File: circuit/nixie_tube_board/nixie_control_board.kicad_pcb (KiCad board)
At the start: 4 copper layers, 200 x 63 mm, 11 parts, among them P5 CONN_01X08, P6 CONN_01X12, U10 IN-14, U11 IN-14, U12 IN-14, U13 IN-14, U14 IN-14, U15 IN-14, U16 IN-14, U17 IN-14

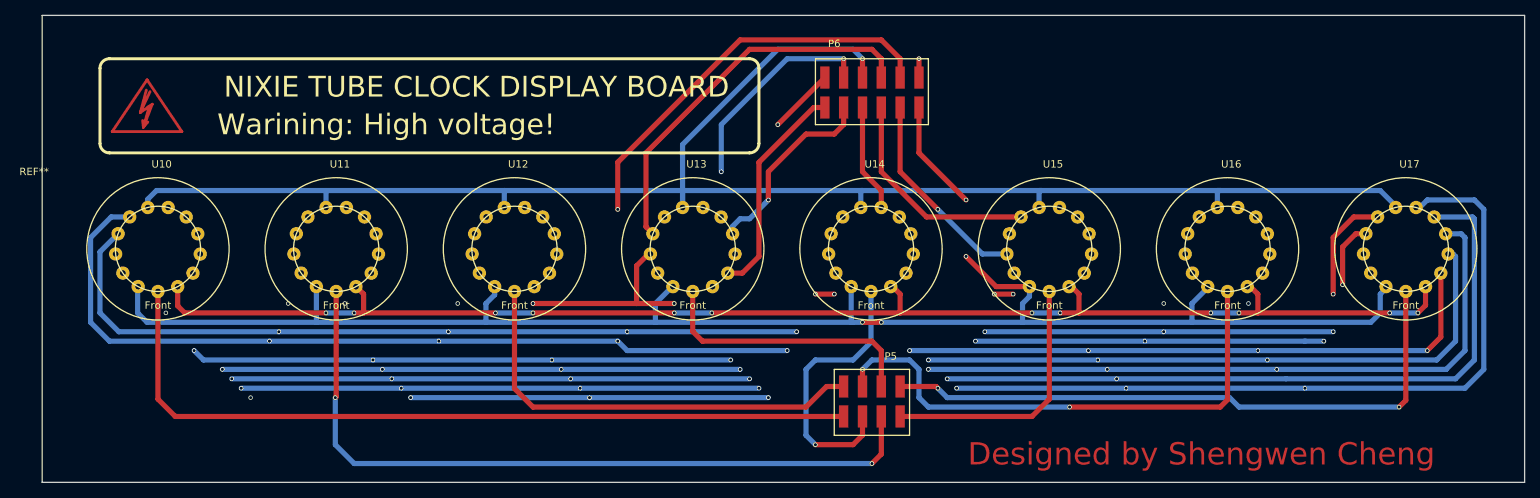
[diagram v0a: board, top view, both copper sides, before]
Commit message: New hardware is almost finished
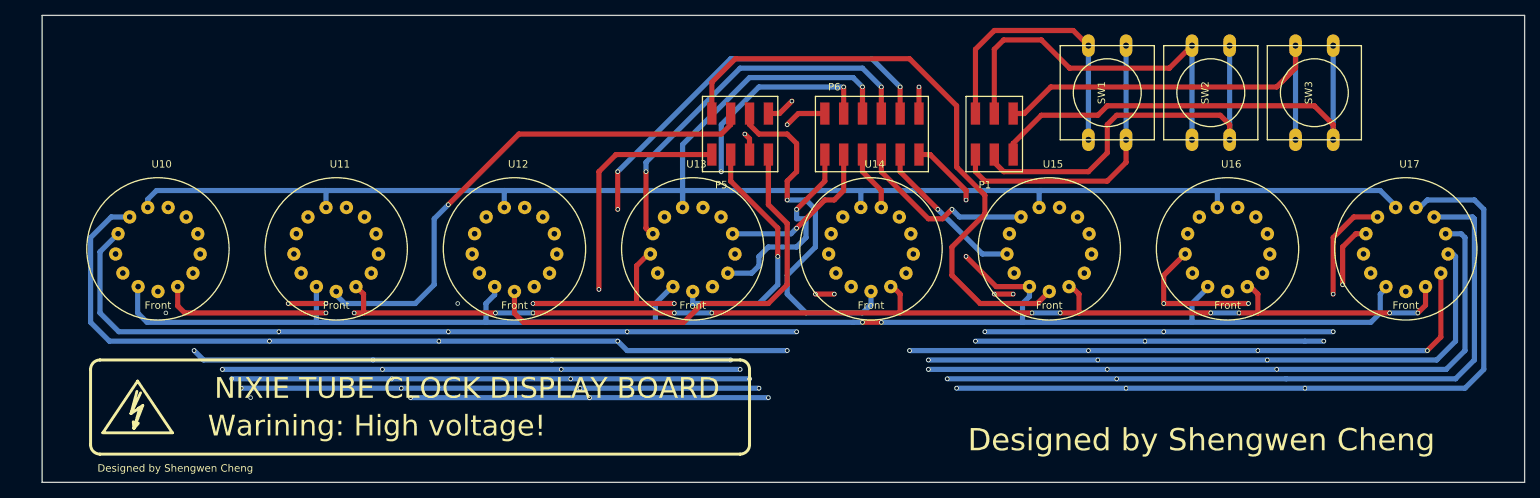
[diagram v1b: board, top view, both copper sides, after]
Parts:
- removed REF**: Symbol_HighVoltage_Type2_CopperTop_VerySmall, Symbols:Symbol_HighVoltage_Type2_CopperTop_VerySmall
- added Designed by Shengwen Cheng: Symbol_HighVoltage_Type2_CopperTop_VerySmall, warning:warning, F.Cu at (65.0, 124.1)
- added P1: CONN_02X03, SMD_PIN_2_BY_3:SMD_PIN_2_BY_3, F.Cu at (178.0, 85.3)
- added SW1: SW_PUSH, Buttons_Switches_ThroughHole:SW_PUSH-12mm, F.Cu at (195.8, 81.0)
- added SW2: SW_PUSH, Buttons_Switches_ThroughHole:SW_PUSH-12mm, F.Cu at (209.7, 81.0)
- added SW3: SW_PUSH, Buttons_Switches_ThroughHole:SW_PUSH-12mm, F.Cu at (223.7, 81.0)
- moved P5 46.9 mm to (142.4, 85.3), turned to 0 degrees
- moved P6 6.35 mm to (157.7, 85.3)
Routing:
- net anode8: track 84.4 -> 168.3 mm, vias 2 -> 1
- net Net-(P1-Pad5): track 0.00 -> 62.6 mm
- net Net-(P1-Pad6): track 0.00 -> 56.4 mm
- net Net-(P1-Pad3): track 0.00 -> 54.0 mm
- net Net-(P1-Pad4): track 0.00 -> 51.4 mm
- net anode7: track 35.6 -> 82.8 mm
- net Net-(P1-Pad1): track 0.00 -> 39.9 mm
- net Net-(P1-Pad2): track 0.00 -> 38.5 mm
- net anode5: track 101.0 -> 70.9 mm, vias 2 -> 1
- net anode4: track 72.0 -> 96.7 mm, vias 2 -> 1
- net anode3: track 37.2 -> 49.0 mm
- net cathode6: track 452.8 -> 446.5 mm
- net cathode2: track 257.0 -> 251.1 mm
- net cathode4: track 365.2 -> 359.9 mm, vias 8 -> 9
- net cathode_comma_left: track 241.1 -> 236.0 mm
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
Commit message: Create footprint common library
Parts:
- removed Designed by Shengwen Cheng: Symbol_HighVoltage_Type2_CopperTop_VerySmall, warning:warning
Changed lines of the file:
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@@
     (links 116)
     (no_connects 3)
-    (area 48.908353 70.493439 252.145001 133.643441)
+    (area 51.994999 70.493439 252.145001 133.643441)
     (thickness 1.6)
     (drawings 15)
     (tracks 738)
     (zones 0)
-    (modules 15)
+    (modules 14)
     (nets 27)
   )
@@
       (net 13 cathode9))
   )
-  (module warning:warning (layer F.Cu)
-    (at 64.95288 124.09)
-    (descr "Symbol, High Voltage, Type 2, Copper Top, Very Small,")
-    (tags "Symbol, High Voltage, Type 2, Copper Top, Very Small,")
-    (fp_text reference "Designed by Shengwen Cheng" (at 5.08 7.57344) (layer F.SilkS)
-      (effects (font (size 1 1) (thickness 0.15)))
-    )
-    (fp_text value Symbol_HighVoltage_Type2_CopperTop_VerySmall (at 2.54 -10.16) (layer F.Fab)
-      (effects (font (size 1 1) (thickness 0.15)))
-    )
-    (fp_line (start -0.49784 2.19964) (end 0.70104 -0.89916) (layer F.SilkS) (width 0.381))
-    (fp_line (start 0.70104 -0.89916) (end 0.1016 -0.50038) (layer F.SilkS) (width 0.381))
-    (fp_line (start -0.89916 0.20066) (end 0.40132 -2.60096) (layer F.SilkS) (width 0.381))
-    (fp_line (start -0.49784 2.19964) (end 0.1016 1.50114) (layer F.SilkS) (width 0.381))
-    (fp_line (start -0.09906 -2.79908) (end -0.89916 0.20066) (layer F.SilkS) (width 0.381))
-    (fp_line (start -0.89916 0.20066) (end 0.29972 -0.59944) (layer F.SilkS) (width 0.381))
-    (fp_line (start 0.29972 -0.59944) (end -0.49784 2.19964) (layer F.SilkS) (width 0.381))
-    (fp_line (start -0.49784 2.19964) (end -0.59944 1.30048) (layer F.SilkS) (width 0.381))
-    (fp_line (start 0 -4.191) (end 4.699 2.794) (layer F.SilkS) (width 0.381))
-    (fp_line (start 4.699 2.794) (end -4.699 2.794) (layer F.SilkS) (width 0.381))
-    (fp_line (start -4.699 2.794) (end 0 -4.191) (layer F.SilkS) (width 0.381))
-  )
   (module IN-14:IN-14 (layer F.Cu)
